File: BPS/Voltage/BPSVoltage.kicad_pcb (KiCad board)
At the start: 2 copper layers, 75 x 65 mm, 124 parts, among them J1 Conn1, J2 Conn2, J3 Conn_01x06, J4 Conn_01x07, J5 Conn_01x03, J6 Conn_01x05, J7 Conn_01x05, Q1 BSS308PE, Q10 BSS308PE, Q11 BSS308PE, Q12 BSS308PE, Q13 BSS308PE, Q2 BSS308PE, Q3 BSS308PE, Q4 BSS308PE, Q5 NSV1C201MZ4, Q6 BSS308PE, Q7 BSS308PE, Q8 BSS308PE, Q9 BSS308PE, U1 LTC6811-1, U2 HX1188FNL

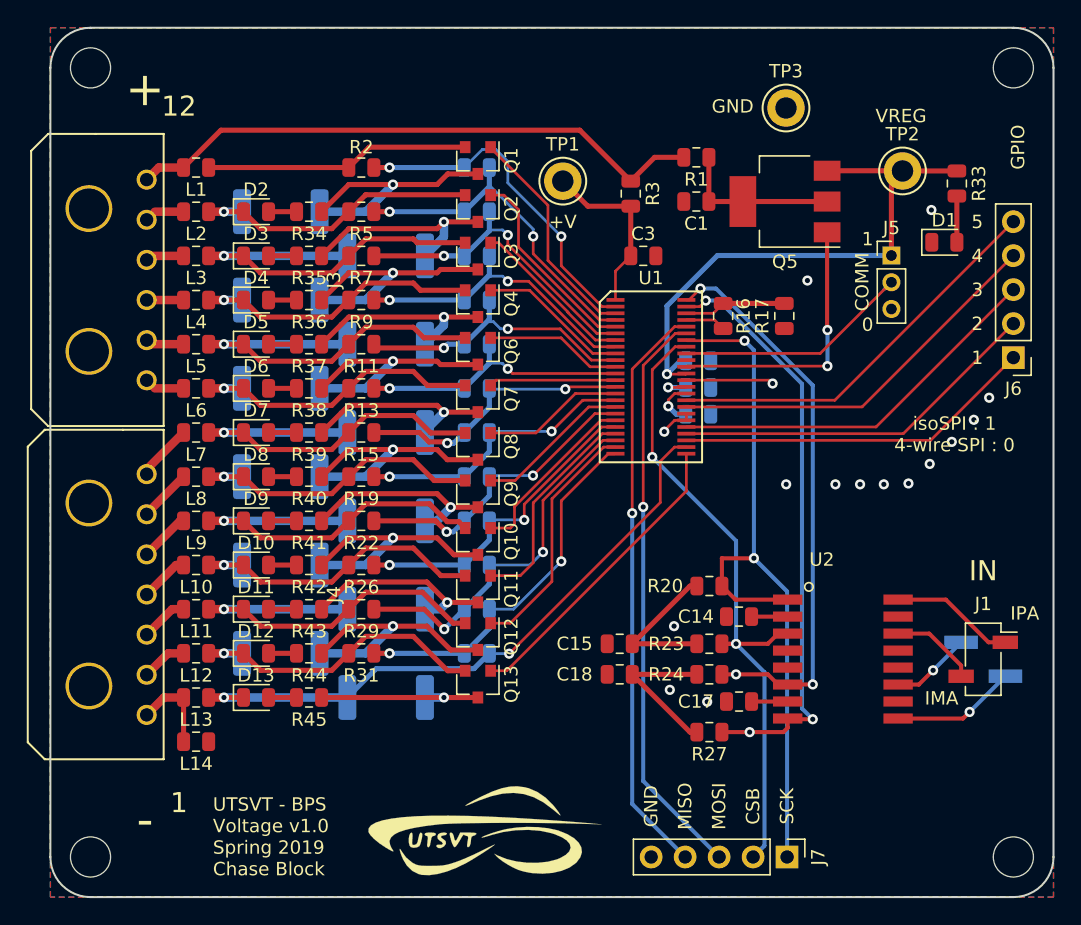
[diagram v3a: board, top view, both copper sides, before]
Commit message: Updated LTC6811 footprint.
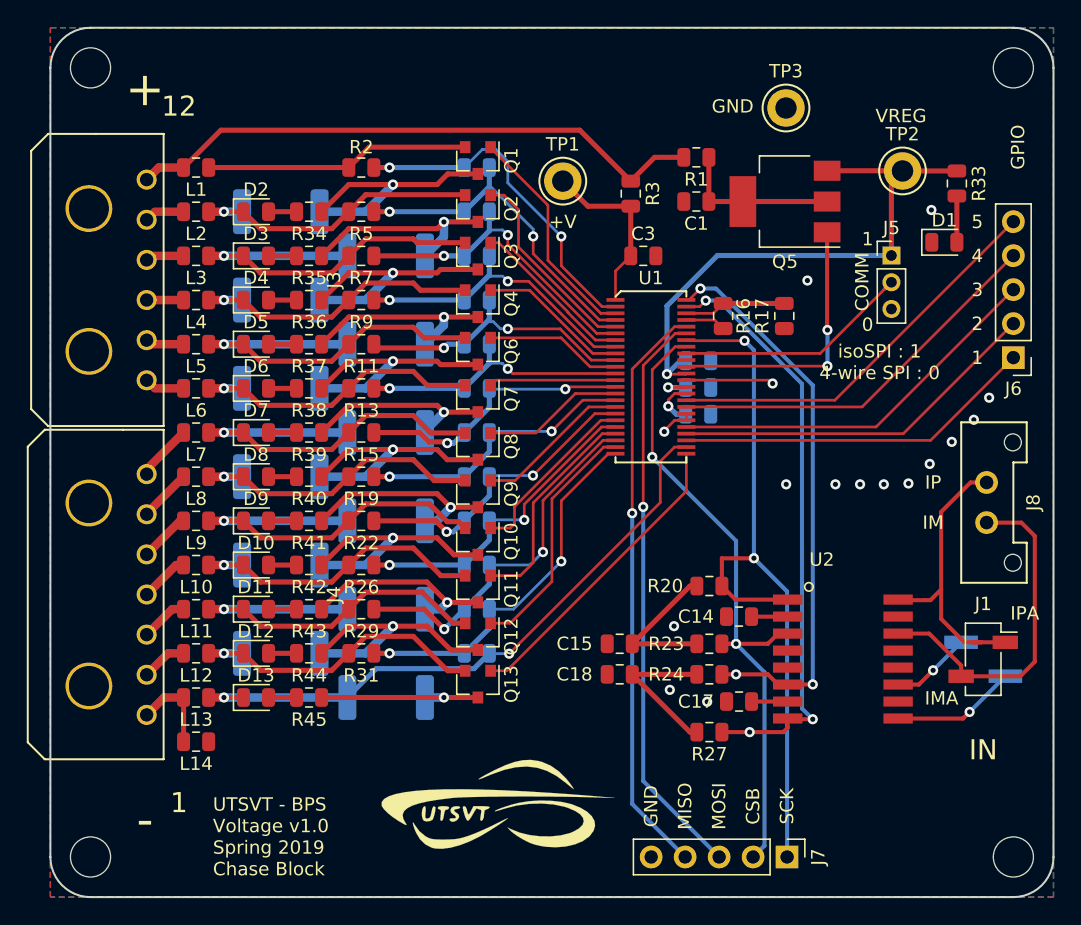
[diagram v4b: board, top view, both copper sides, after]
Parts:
- removed ? (x4): MountingHole, MountingHole:MountingHole_3mm
- added J8: Conn_01x02, UTSVT_Connectors:Molex_MicroFit3.0_1x2xP3.00mm_PolarizingPeg_Vertical, F.Cu at (115.0, 84.0)
- added MH1: MountingHole, MountingHole:MountingHole_3mm, F.Cu at (48.0, 112.0)
- added MH2: MountingHole, MountingHole:MountingHole_3mm, F.Cu at (117.0, 53.0)
- added MH3: MountingHole, MountingHole:MountingHole_3mm, F.Cu at (117.0, 112.0)
- added MH4: MountingHole, MountingHole:MountingHole_3mm, F.Cu at (48.0, 53.0)
- moved G*** 2.20 mm to (78.2, 108.2)
- moved G*** 0.27 mm to (102.2, 91.6)
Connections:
- U1 pad 39: (no net) -> Net-(U1-Pad39)
- U2 pad 10: (no net) -> Net-(U2-Pad10)
- U2 pad 15: (no net) -> Net-(U2-Pad15)
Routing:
- net Net-(J1-Pad2): track 6.51 -> 25.9 mm
- net Net-(J1-Pad1): track 9.33 -> 22.0 mm
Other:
- board text added: "IM"
- board text added: "IP"

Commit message: footprint error fixed in voltage board. Created new gerber files.
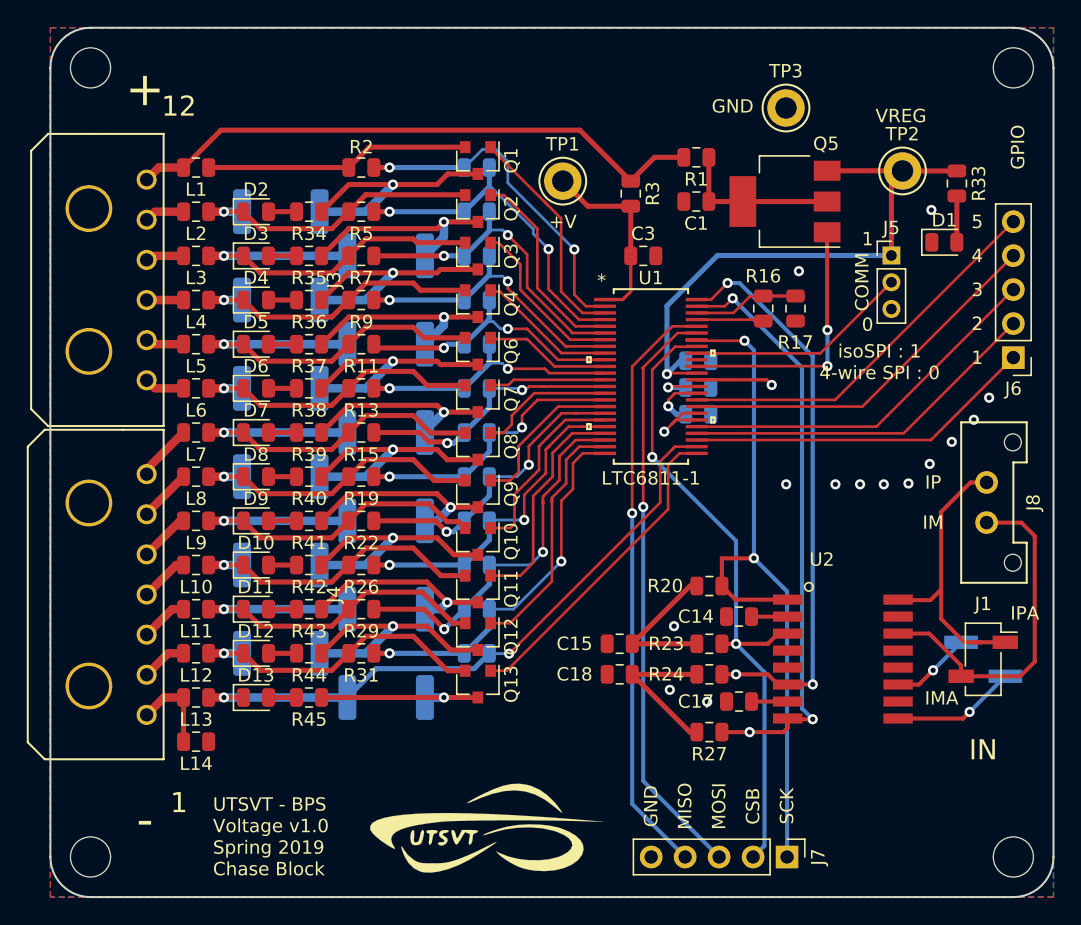
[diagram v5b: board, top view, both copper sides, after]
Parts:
- U1: footprint UTSVT_ICs:SOIC-48 -> UTSVT_BPS:LTC6811HG-1-PBF
- moved R16 3.05 mm to (98.3, 71.0)
- moved G*** 1.98 mm to (77.3, 110.0)
- moved R17 1.01 mm to (100.7, 71.0)
- moved G*** 0.47 mm to (102.0, 91.2)
- turned U1 to 0 degrees
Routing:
- net Net-(R16-Pad2): track 3.01 -> 5.05 mm
- net GND: track 9.10 -> 10.8 mm
- net Net-(Q13-Pad1): track 23.0 -> 24.1 mm
- net Net-(C3-Pad1): track 13.3 -> 14.4 mm
- net /Batt0: track 46.8 -> 47.8 mm
- net Net-(Q10-Pad1): track 13.4 -> 14.4 mm
- net Net-(C8-Pad1): track 3.57 -> 4.51 mm
- net /SDO: track 43.5 -> 44.4 mm
- net Net-(C16-Pad1): track 23.9 -> 24.7 mm
- net Net-(Q7-Pad1): track 9.50 -> 8.65 mm
- net /IPB: track 42.3 -> 43.1 mm
- net Net-(C9-Pad1): track 2.70 -> 3.49 mm
- net /GPIO5: track 30.0 -> 29.2 mm
- net /GPIO2: track 27.9 -> 27.1 mm
- net Net-(C6-Pad1): track 23.3 -> 22.5 mm
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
